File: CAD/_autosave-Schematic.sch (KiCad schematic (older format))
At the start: 7 parts

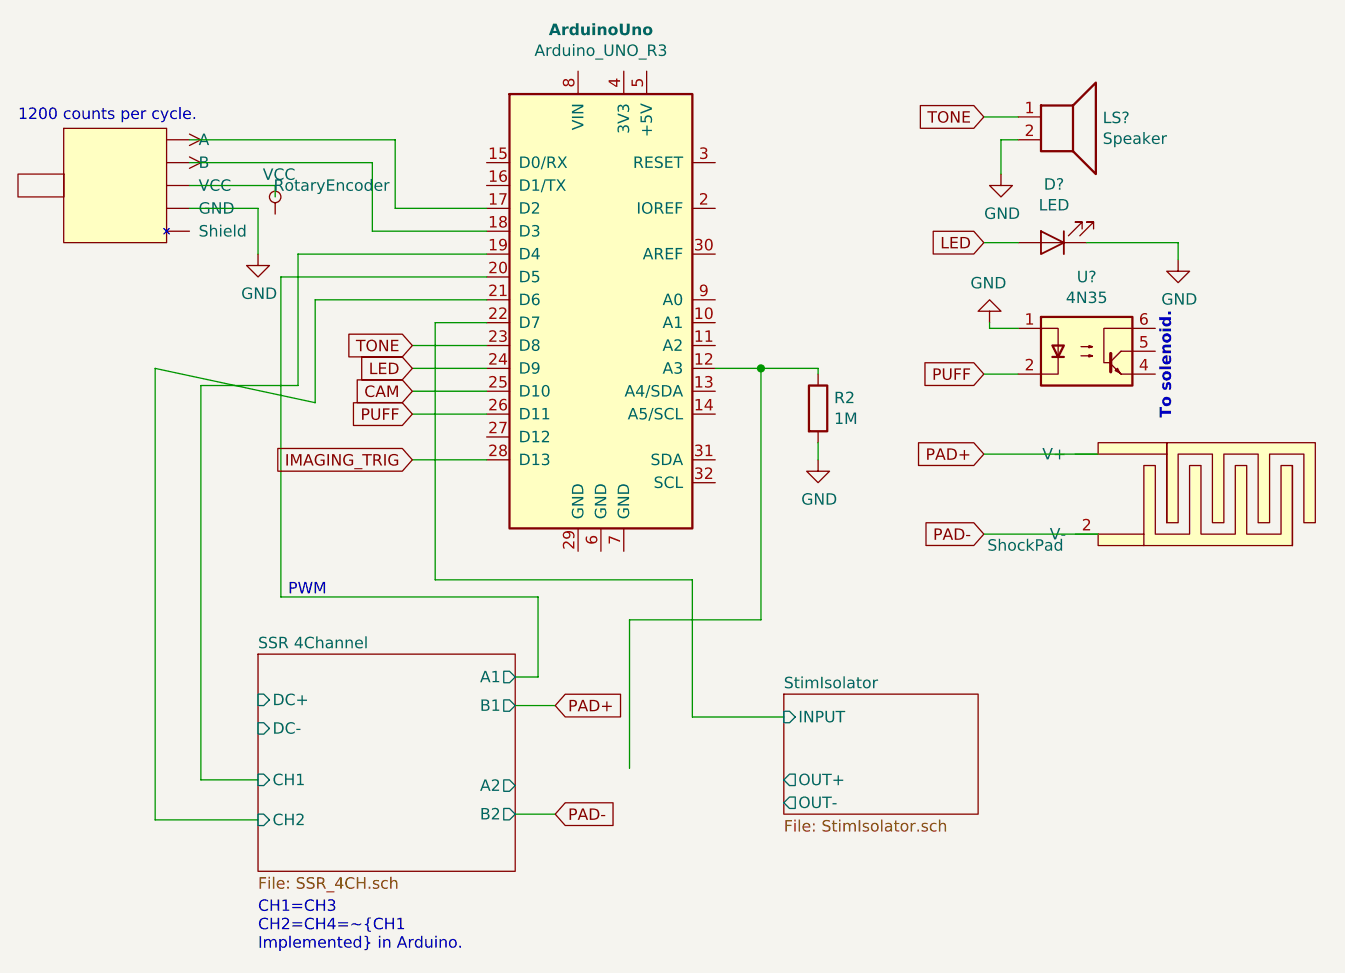
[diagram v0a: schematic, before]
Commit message: Added missing projects.
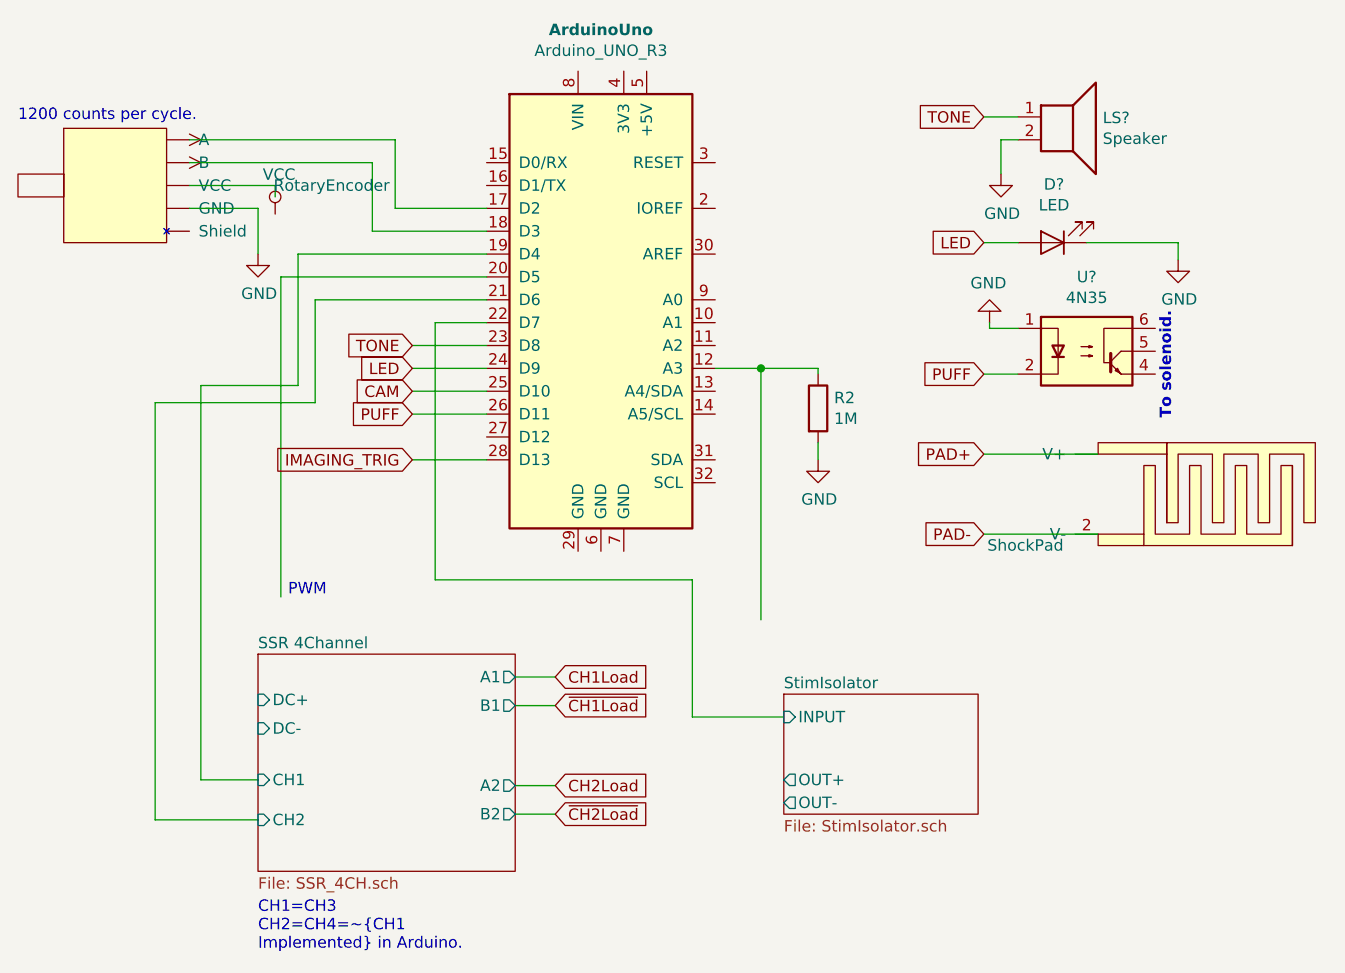
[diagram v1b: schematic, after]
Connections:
- net labels added: CH1Load, CH2Load, ~CH1Load, ~CH2Load
- wire segments 55 -> 52
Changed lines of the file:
@@
 	5550 3200 5550 3650
-Wire Wire Line
-	5550 3650 4850 3500
 Wire Wire Line
 	5550 3200 6300 3200
 Wire Wire Line
 	5400 3100 5400 4500
-Wire Wire Line
-	5400 4500 6525 4500
-Wire Wire Line
-	6525 4500 6525 4850
-Wire Wire Line
-	6525 4850 6425 4850
 Wire Wire Line
 	5400 3100 6300 3100
@@
 Wire Wire Line
 	8475 4225 8975 4225
-Text GLabel 6600 4975 2    50   Input ~ 0
-PAD+
 Wire Wire Line
 	7200 4425 7200 5025
@@
 Wire Wire Line
 	6075 4425 7200 4425
-Wire Wire Line
-	6925 5250 6925 4600
-Wire Wire Line
-	6925 4600 7500 4600
 Wire Wire Line
 	7500 4600 7500 3500
@@
 Wire Wire Line
 	5300 5475 4850 5475
-Wire Wire Line
-	4850 3500 4850 5475
-Text GLabel 6600 5450 2    50   Input ~ 0
-PAD-
 $Sheet
 S 5300 4750 1125 950
@@
 Wire Wire Line
 	6425 4975 6600 4975
+Wire Wire Line
+	5550 3650 4850 3650
+Wire Wire Line
+	4850 3650 4850 5475
+Text GLabel 6600 4850 2    50   Input ~ 0
+CH1Load
+Wire Wire Line
+	6600 4850 6425 4850
+Text GLabel 6600 4975 2    50   Input ~ 0
+~CH1Load
+Text GLabel 6600 5325 2    50   Input ~ 0
+CH2Load
+Text GLabel 6600 5450 2    50   Input ~ 0
+~CH2Load
+Wire Wire Line
+	6425 5325 6600 5325
 $EndSCHEMATC
